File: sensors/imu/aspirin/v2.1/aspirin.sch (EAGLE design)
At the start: 23 parts, among them IC1 LP2992, IC2 MS5611, IC3 >4KBIT SERIAL EEPROM HALF PRO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, U1 HMC5883, U2 MPU-6000

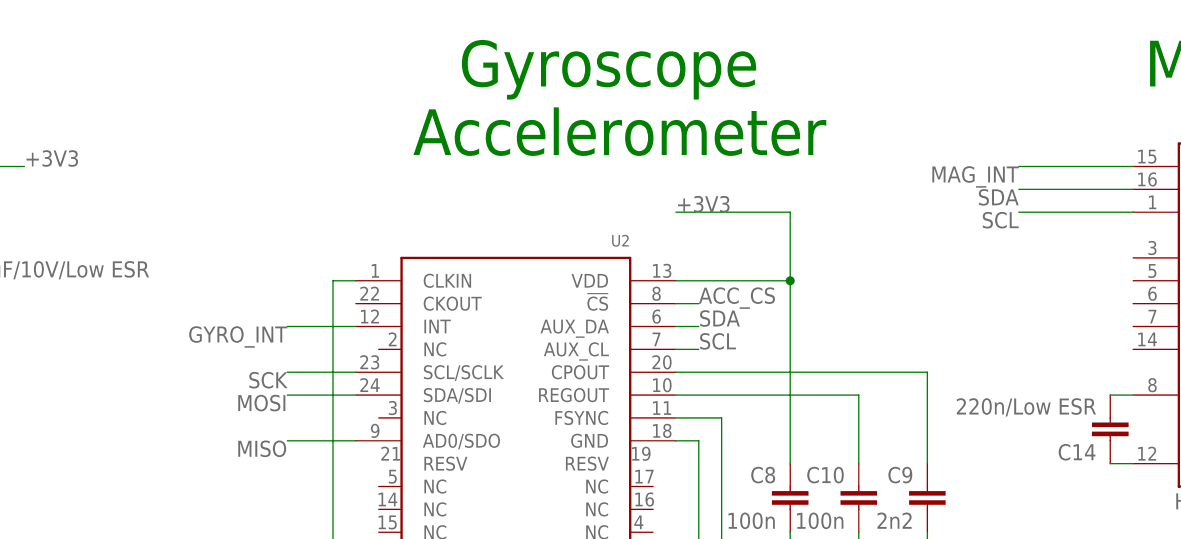
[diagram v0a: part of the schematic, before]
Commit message: Aspirin alt design is cleaner, made it the official routing of v2.1.
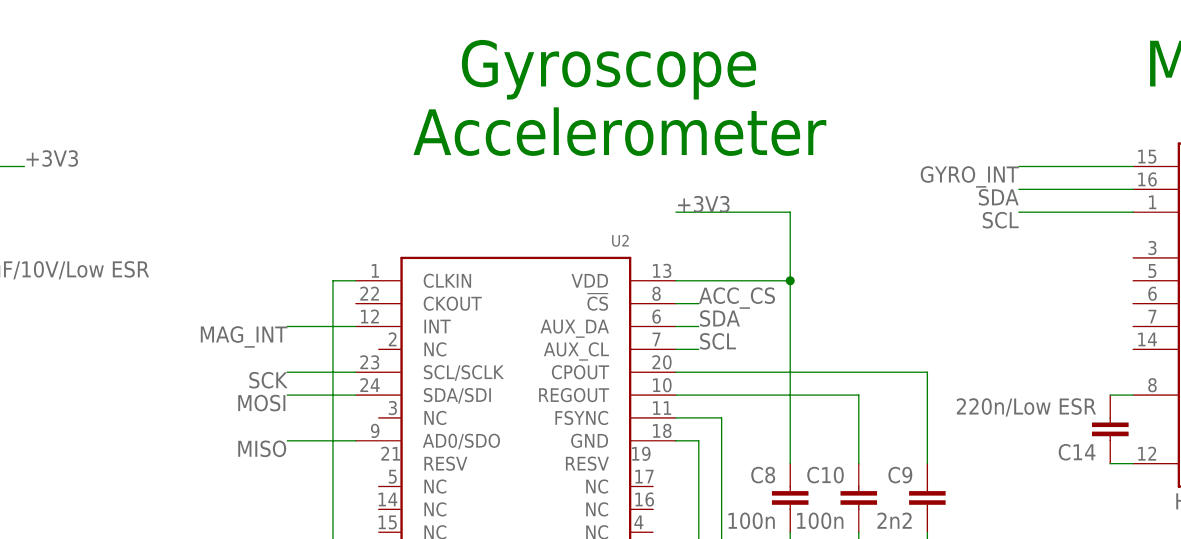
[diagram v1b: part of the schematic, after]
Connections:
- net GYRO_INT: now also U1.DRDY; no longer U2.INT
- net MAG_INT: now also U2.INT; no longer U1.DRDY
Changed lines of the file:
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@@
 <net name="GYRO_INT" class="0">
-<segment>
-<wire x1="106.68" y1="142.24" x2="99.06" y2="142.24" width="0.1524" layer="91"/>
-<label x="99.06" y="142.24" size="1.778" layer="95" rot="R180"/>
-<pinref part="U2" gate="G1" pin="INT"/>
-</segment>
 <segment>
 <wire x1="109.22" y1="53.34" x2="114.3" y2="53.34" width="0.1524" layer="91"/>
 <label x="114.3" y="53.34" size="1.778" layer="95"/>
 <pinref part="ASP1" gate="G$1" pin="GYRO_INT"/>
+</segment>
+<segment>
+<wire x1="193.04" y1="160.02" x2="180.34" y2="160.02" width="0.1524" layer="91"/>
+<label x="180.34" y="160.02" size="1.778" layer="95" rot="R180"/>
+<pinref part="U1" gate="G$1" pin="DRDY"/>
 </segment>
 </net>
@@
 <net name="MAG_INT" class="0">
 <segment>
-<wire x1="193.04" y1="160.02" x2="180.34" y2="160.02" width="0.1524" layer="91"/>
-<label x="180.34" y="160.02" size="1.778" layer="95" rot="R180"/>
-<pinref part="U1" gate="G$1" pin="DRDY"/>
-</segment>
-<segment>
 <wire x1="73.66" y1="53.34" x2="68.58" y2="53.34" width="0.1524" layer="91"/>
 <label x="68.58" y="53.34" size="1.778" layer="95" rot="MR0"/>
 <pinref part="ASP1" gate="G$1" pin="MAG_INT"/>
 </segment>
+<segment>
+<wire x1="106.68" y1="142.24" x2="99.06" y2="142.24" width="0.1524" layer="91"/>
+<label x="99.06" y="142.24" size="1.778" layer="95" rot="R180"/>
+<pinref part="U2" gate="G1" pin="INT"/>
+</segment>
 </net>

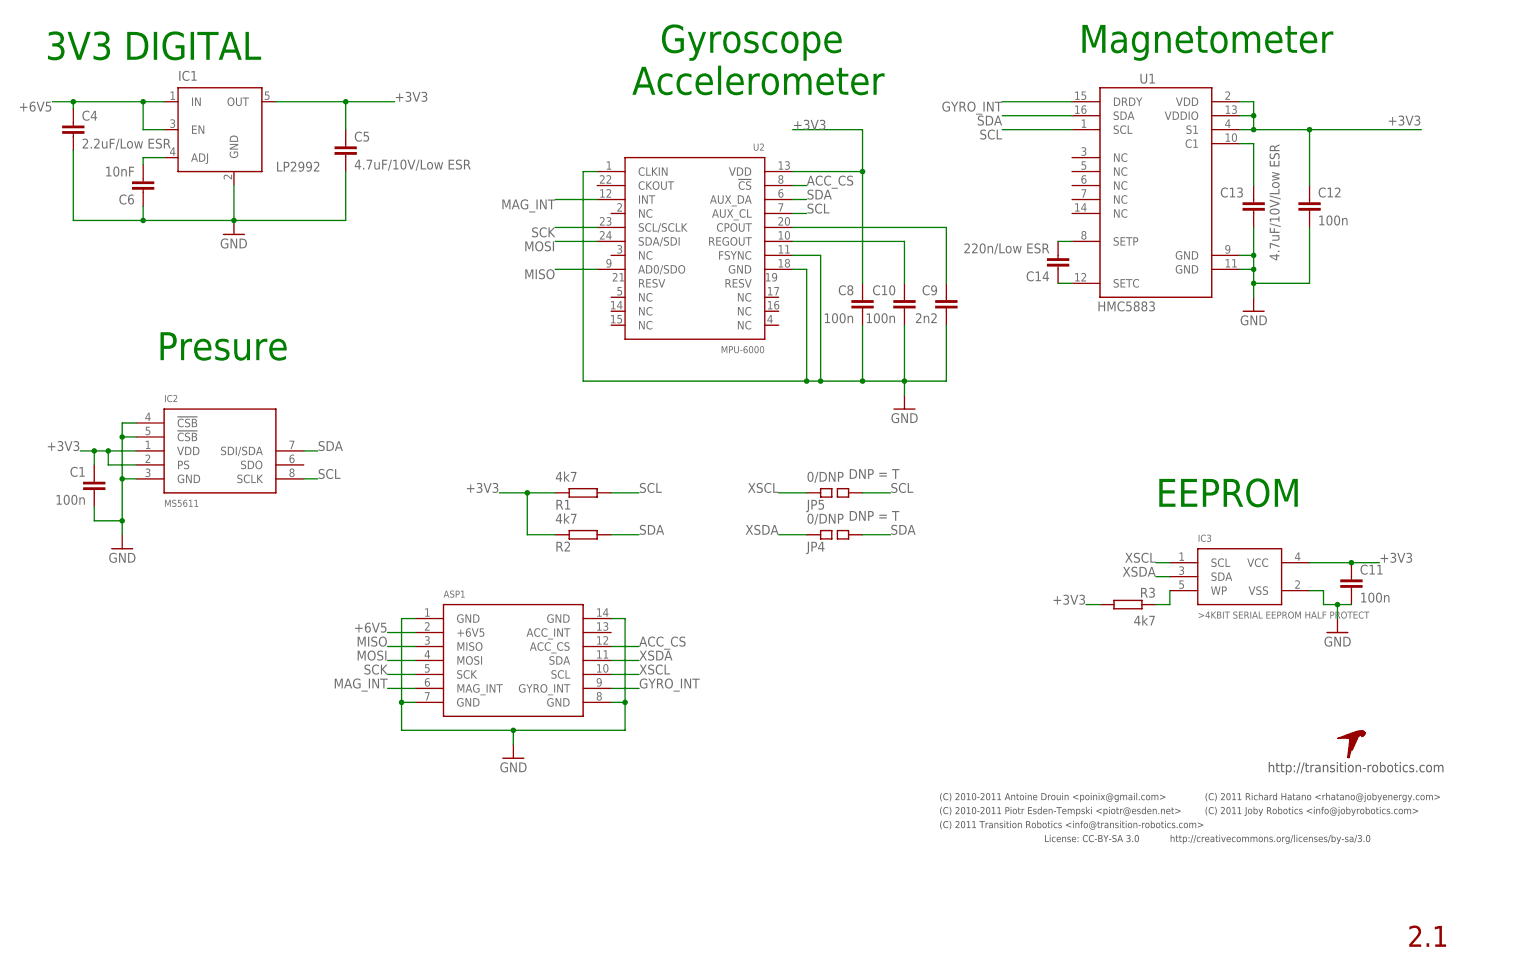
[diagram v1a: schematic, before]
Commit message: Some minor cleanups and touchups. Renamed signal silkscreen legend's to better reflect reality.
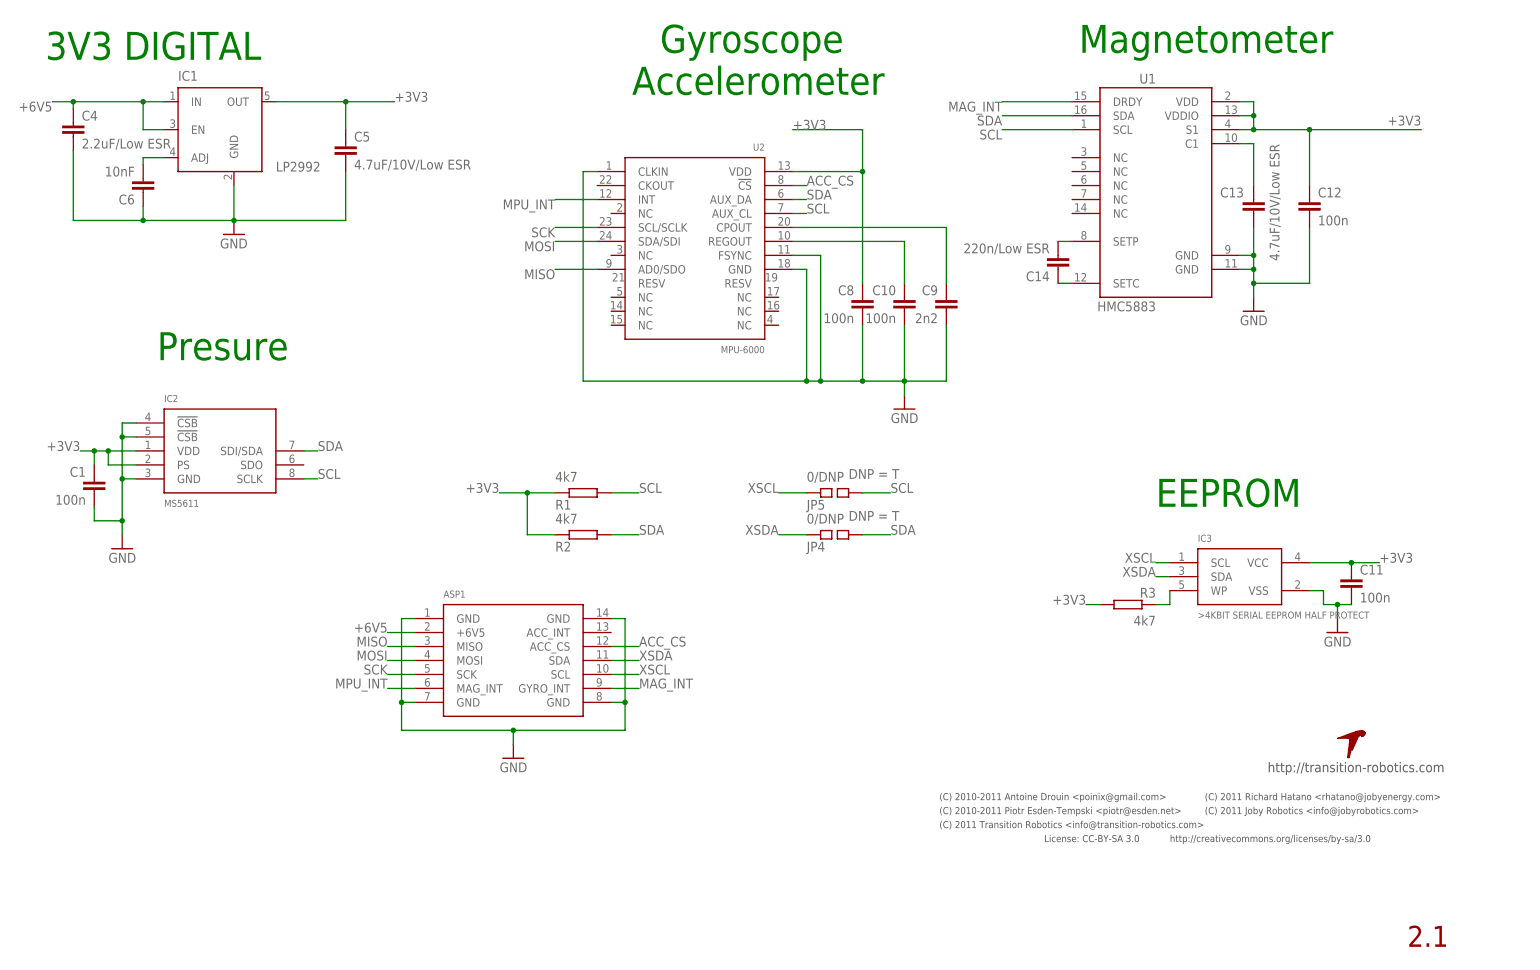
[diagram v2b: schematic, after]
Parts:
- C5: device pel_dipol_comp:CAPACITOR-0402 -> pel_dipol_comp:CAPACITOR-0603
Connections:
- removed net GYRO_INT: ASP1.GYRO_INT, U1.DRDY
- new net MPU_INT: ASP1.MAG_INT, U2.INT
- net MAG_INT: now also ASP1.GYRO_INT, U1.DRDY; no longer ASP1.MAG_INT, U2.INT
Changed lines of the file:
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@@
 <attribute name="PARTNO" value="cap-cer-0603-2u2"/>
 </part>
-<part name="C5" library="pel_dipol_comp" deviceset="CAPACITOR" device="-0402" value="4.7uF/10V/Low ESR">
+<part name="C5" library="pel_dipol_comp" deviceset="CAPACITOR" device="-0603" value="4.7uF/10V/Low ESR">
 <attribute name="PARTNO" value="cap-cer-0402-4n7"/>
 </part>
@@
 <instances>
 <instance part="IC1" gate="G1" x="38.1" y="154.94">
-<attribute name="PARTNO" x="38.1" y="154.94" size="1.778" layer="96" display="off"/>
+<attribute name="PARTNO" value="vreg-sot-23-5-3v3" x="38.1" y="154.94" size="1.778" layer="96" display="off"/>
 </instance>
 <instance part="C6" gate="G$1" x="24.13" y="143.51" rot="R180">
-<attribute name="PARTNO" x="24.13" y="143.51" size="1.778" layer="96" display="off"/>
+<attribute name="PARTNO" value="cap-cer-0402-10n" x="24.13" y="143.51" size="1.778" layer="96" display="off"/>
 </instance>
 <instance part="GND11" gate="1" x="40.64" y="135.89"/>
 <instance part="C4" gate="G$1" x="11.43" y="156.21">
-<attribute name="PARTNO" x="11.43" y="156.21" size="1.778" layer="96" display="off"/>
+<attribute name="PARTNO" value="cap-cer-0603-2u2" x="11.43" y="156.21" size="1.778" layer="96" display="off"/>
 </instance>
 <instance part="C5" gate="G$1" x="60.96" y="152.4">
-<attribute name="PARTNO" x="60.96" y="152.4" size="1.778" layer="96" display="off"/>
+<attribute name="PARTNO" value="cap-cer-0603-4u7" x="60.96" y="152.4" size="1.778" layer="96" display="off"/>
 </instance>
 <instance part="GND1" gate="1" x="162.56" y="104.14" rot="MR0"/>
 <instance part="C8" gate="G$1" x="154.94" y="124.46" rot="MR0">
-<attribute name="PARTNO" x="154.94" y="124.46" size="1.778" layer="96" display="off"/>
+<attribute name="PARTNO" value="cap-cer-0402-100n" x="154.94" y="124.46" size="1.778" layer="96" display="off"/>
 </instance>
 <instance part="C9" gate="G$1" x="170.18" y="124.46" rot="MR0">
-<attribute name="PARTNO" x="170.18" y="124.46" size="1.778" layer="96" display="off"/>
+<attribute name="PARTNO" value="cap-cer-0402-2n2" x="170.18" y="124.46" size="1.778" layer="96" display="off"/>
 </instance>
 <instance part="C10" gate="G$1" x="162.56" y="124.46" rot="MR0">
-<attribute name="PARTNO" x="162.56" y="124.46" size="1.778" layer="96" display="off"/>
+<attribute name="PARTNO" value="cap-cer-0402-100n" x="162.56" y="124.46" size="1.778" layer="96" display="off"/>
 </instance>
 <instance part="C13" gate="G$1" x="226.06" y="142.24" smashed="yes">
 <attribute name="NAME" x="219.964" y="142.621" size="1.778" layer="95"/>
 <attribute name="VALUE" x="230.759" y="131.064" size="1.778" layer="96" rot="R90"/>
-<attribute name="PARTNO" x="226.06" y="142.24" size="1.778" layer="96" display="off"/>
+<attribute name="PARTNO" value="cap-cer-0603-4u7" x="226.06" y="142.24" size="1.778" layer="96" display="off"/>
 </instance>
 <instance part="GND10" gate="1" x="226.06" y="121.92" rot="MR0"/>
 <instance part="C14" gate="G$1" x="190.5" y="129.54" rot="R180">
-<attribute name="PARTNO" x="190.5" y="129.54" size="1.778" layer="96" display="off"/>
+<attribute name="PARTNO" value="cap-cer-0603-220n" x="190.5" y="129.54" size="1.778" layer="96" display="off"/>
 </instance>
 <instance part="C12" gate="G$1" x="236.22" y="142.24">
-<attribute name="PARTNO" x="236.22" y="142.24" size="1.778" layer="96" display="off"/>
+<attribute name="PARTNO" value="cap-cer-0402-100n" x="236.22" y="142.24" size="1.778" layer="96" display="off"/>
 </instance>
 <instance part="IC3" gate="G$1" x="223.52" y="73.66">
-<attribute name="PARTNO" x="223.52" y="73.66" size="1.778" layer="96" display="off"/>
+<attribute name="PARTNO" value="ic-sot-23-5-4k-eeprom" x="223.52" y="73.66" size="1.778" layer="96" display="off"/>
 </instance>
 <instance part="C11" gate="G$1" x="243.84" y="73.66">
-<attribute name="PARTNO" x="243.84" y="73.66" size="1.778" layer="96" display="off"/>
+<attribute name="PARTNO" value="cap-cer-0402-100n" x="243.84" y="73.66" size="1.778" layer="96" display="off"/>
 </instance>
 <instance part="GND2" gate="1" x="241.3" y="63.5" rot="MR0"/>
@@
 <instance part="FRAME2" gate="G$2" x="162.56" y="0"/>
 <instance part="U1" gate="G$1" x="208.28" y="144.78">
-<attribute name="PARTNO" x="208.28" y="144.78" size="1.778" layer="96" display="off"/>
+<attribute name="PARTNO" value="sensr-plcc-16-mag" x="208.28" y="144.78" size="1.778" layer="96" display="off"/>
 </instance>
 <instance part="U2" gate="G1" x="124.46" y="139.7" rot="MR0">
-<attribute name="PARTNO" x="124.46" y="139.7" size="1.778" layer="96" display="off"/>
+<attribute name="PARTNO" value="sensr-qfn-24-acc-gyro" x="124.46" y="139.7" size="1.778" layer="96" display="off"/>
 </instance>
 <instance part="ASP1" gate="G$1" x="91.44" y="58.42">
-<attribute name="PARTNO" x="91.44" y="58.42" size="1.778" layer="96" display="off"/>
+<attribute name="PARTNO" value="pcb-aspirin" x="91.44" y="58.42" size="1.778" layer="96" display="off"/>
 </instance>
 <instance part="GND3" gate="1" x="91.44" y="40.64" rot="MR0"/>
@@
 </instance>
 <instance part="JP5" gate="G$1" x="149.86" y="88.9">
-<attribute name="PARTNO" x="149.86" y="88.9" size="1.778" layer="96" rot="MR90" display="off"/>
+<attribute name="PARTNO" value="res-0402-0" x="149.86" y="88.9" size="1.778" layer="96" rot="MR90" display="off"/>
 <attribute name="DNP" x="152.4" y="91.44" size="1.778" layer="96" display="both"/>
 </instance>
 <instance part="JP4" gate="G$1" x="149.86" y="81.28">
-<attribute name="PARTNO" x="149.86" y="81.28" size="1.778" layer="96" rot="MR90" display="off"/>
+<attribute name="PARTNO" value="res-0402-0" x="149.86" y="81.28" size="1.778" layer="96" rot="MR90" display="off"/>
 <attribute name="DNP" x="152.4" y="83.82" size="1.778" layer="96" display="both"/>
 </instance>
 <instance part="IC2" gate="G$1" x="38.1" y="96.52">
-<attribute name="PARTNO" x="38.1" y="96.52" size="1.778" layer="96" display="off"/>
+<attribute name="PARTNO" value="sensr-qfn-8-baro" x="38.1" y="96.52" size="1.778" layer="96" display="off"/>
 </instance>
 <instance part="C1" gate="G$1" x="15.24" y="91.44" rot="MR0">
-<attribute name="PARTNO" x="15.24" y="91.44" size="1.778" layer="96" display="off"/>
+<attribute name="PARTNO" value="cap-cer-0402-100n" x="15.24" y="91.44" size="1.778" layer="96" display="off"/>
 </instance>
 <instance part="GND4" gate="1" x="20.32" y="78.74" rot="MR0"/>
 <instance part="R1" gate="G$1" x="104.14" y="88.9">
-<attribute name="PARTNO" x="104.14" y="88.9" size="1.778" layer="96" display="off"/>
+<attribute name="PARTNO" value="res-0402-4k7" x="104.14" y="88.9" size="1.778" layer="96" display="off"/>
 </instance>
 <instance part="R2" gate="G$1" x="104.14" y="81.28">
-<attribute name="PARTNO" x="104.14" y="81.28" size="1.778" layer="96" display="off"/>
+<attribute name="PARTNO" value="res-0402-4k7" x="104.14" y="81.28" size="1.778" layer="96" display="off"/>
 </instance>
 <instance part="R3" gate="G$1" x="203.2" y="68.58" rot="R180">
-<attribute name="PARTNO" x="203.2" y="68.58" size="1.778" layer="96" rot="R180" display="off"/>
+<attribute name="PARTNO" value="res-0402-4k7" x="203.2" y="68.58" size="1.778" layer="96" rot="R180" display="off"/>
 </instance>
 </instances>
@@
 </segment>
 </net>
-<net name="GYRO_INT" class="0">
+<net name="MAG_INT" class="0">
 <segment>
 <wire x1="109.22" y1="53.34" x2="114.3" y2="53.34" width="0.1524" layer="91"/>
@@
 </segment>
 </net>
-<net name="MAG_INT" class="0">
+<net name="MPU_INT" class="0">
 <segment>
 <wire x1="73.66" y1="53.34" x2="68.58" y2="53.34" width="0.1524" layer="91"/>

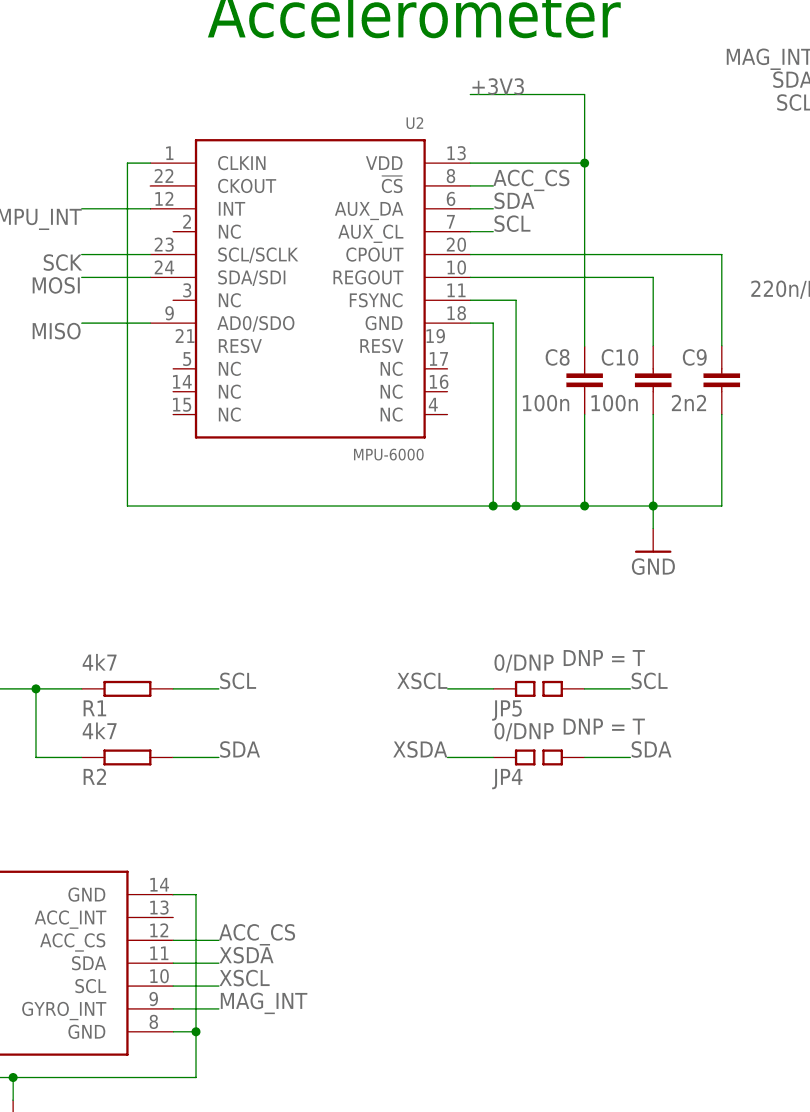
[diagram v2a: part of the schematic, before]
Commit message: Renamed ACC_CS to MPU_CS and changed panel to 3x3.
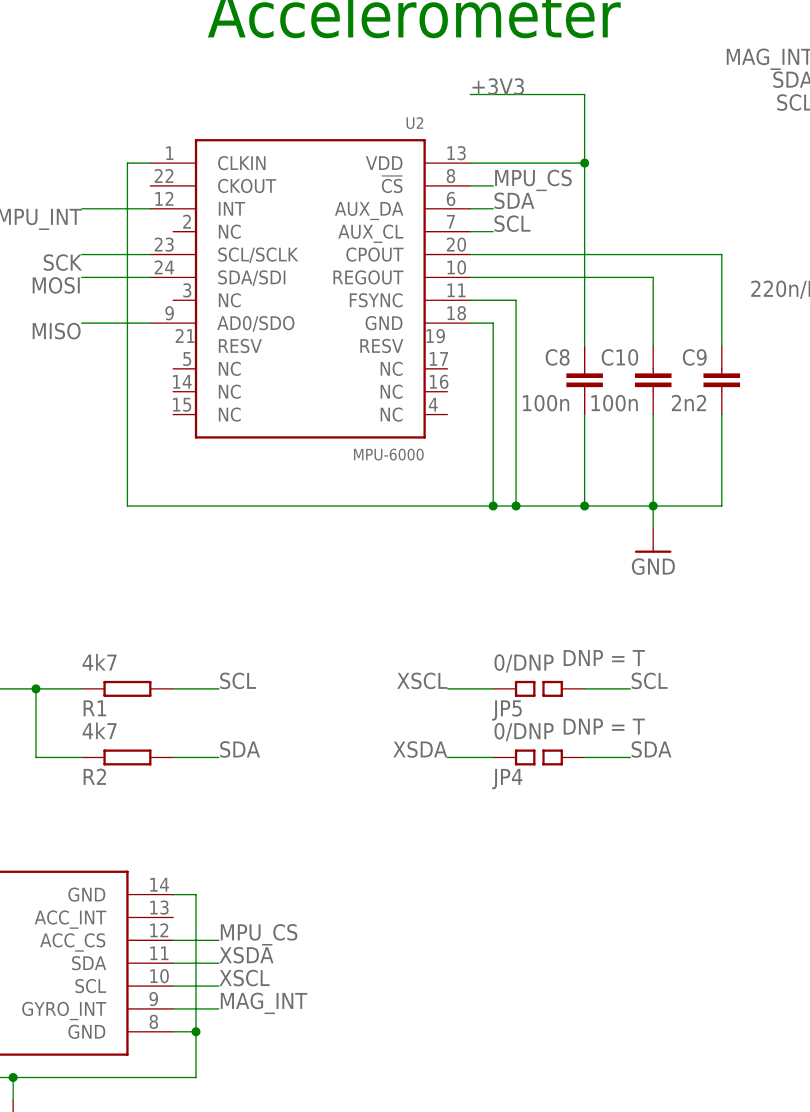
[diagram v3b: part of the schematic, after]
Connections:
- net ACC_CS renamed MPU_CS
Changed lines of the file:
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@@
 </segment>
 </net>
-<net name="ACC_CS" class="0">
+<net name="MPU_CS" class="0">
 <segment>
 <wire x1="142.24" y1="144.78" x2="144.78" y2="144.78" width="0.1524" layer="91"/>
